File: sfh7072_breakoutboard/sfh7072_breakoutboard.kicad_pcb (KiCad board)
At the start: 2 copper layers, 28 x 23 mm, 10 parts, among them J1 Conn_01x04_Pin, J2 Conn_01x05_Pin

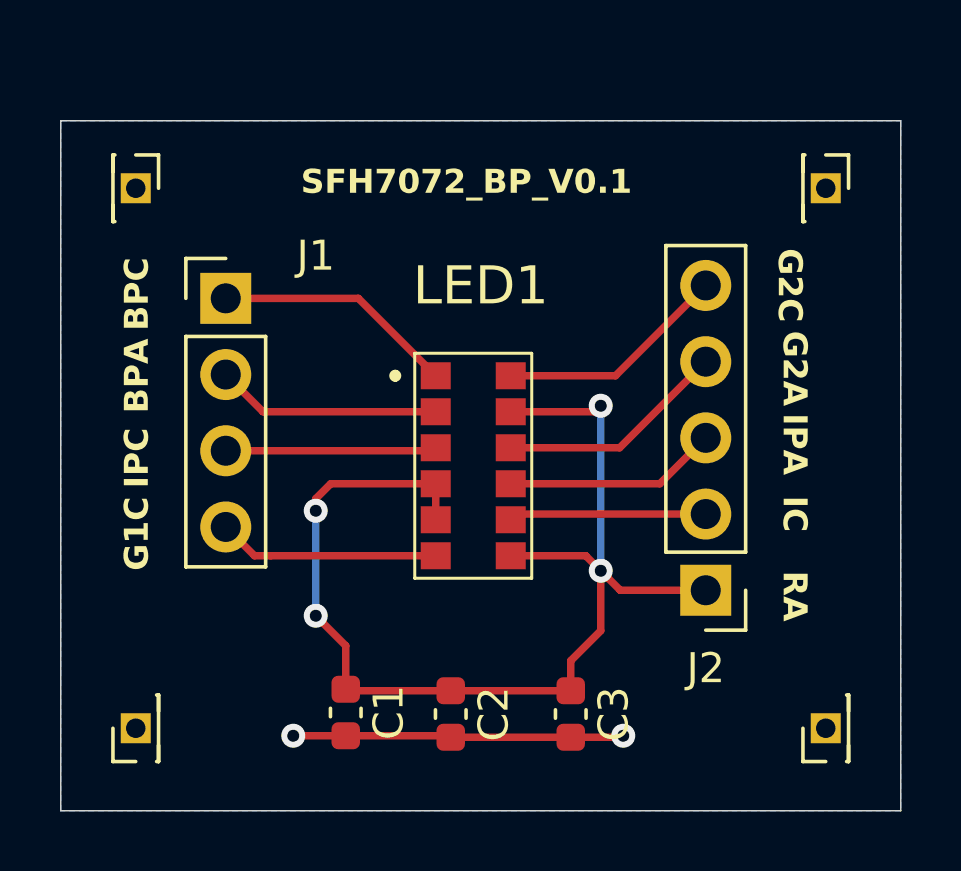
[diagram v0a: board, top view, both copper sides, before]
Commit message: sfh7072 cap location updates
Signed-off-by: Mika Laitio <lamikr@gmail.com>
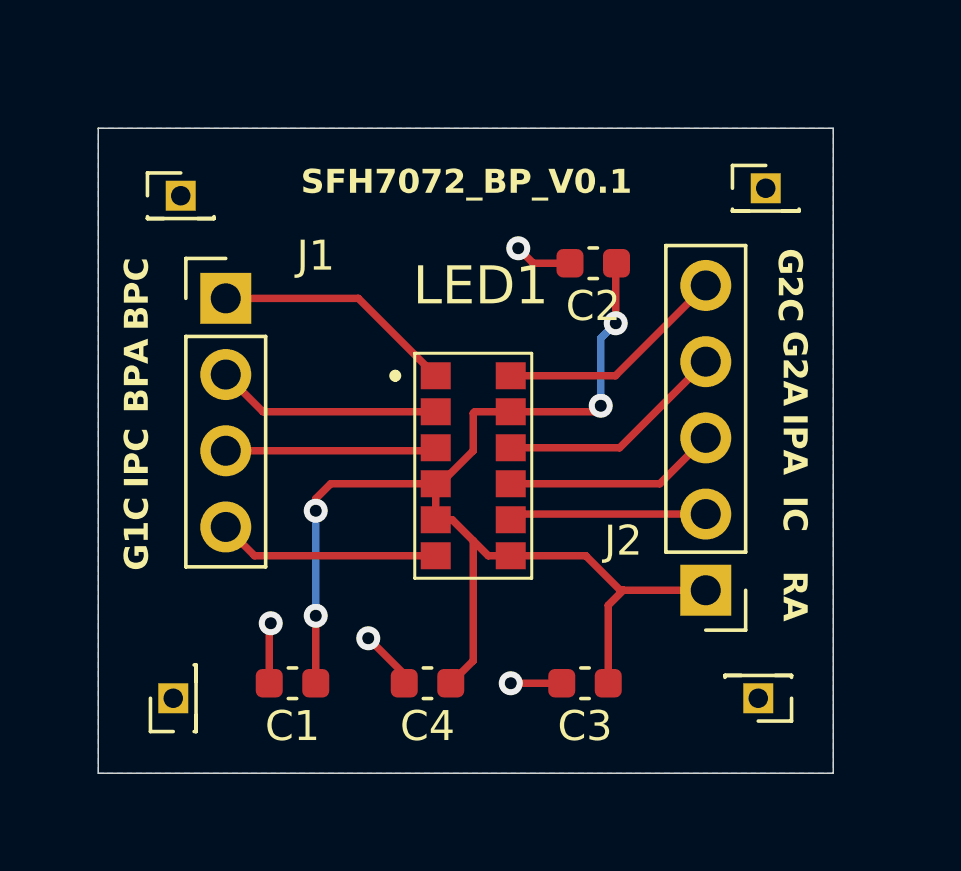
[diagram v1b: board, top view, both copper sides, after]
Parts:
- added C4: 4u7F, Capacitor_SMD:C_0603_1608Metric, F.Cu at (30.7, 35.5)
- moved C2 15.8 mm to (36.2, 21.5), turned to 180 degrees
- moved H3 2.46 mm to (41.8, 36.0), turned to 180 degrees
- moved C1 2.03 mm to (26.2, 35.5), turned to 180 degrees
- moved H2 2.00 mm to (42.0, 19.0), turned to 0 degrees
- moved H4 1.60 mm to (22.2, 36.0)
- moved H1 1.52 mm to (22.5, 19.2), turned to 0 degrees
- moved C3 1.13 mm to (36.0, 35.5), turned to 180 degrees
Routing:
- net GND: track 11.0 -> 7.65 mm, vias 2 -> 4
- net Net-(J2-Pin_1): track 39.7 -> 42.2 mm
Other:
- board size 28 x 23 mm -> 24.5 x 21.5 mm

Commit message: sfh7072 breakoutboard and pcb manufacturing
Signed-off-by: Mika Laitio <lamikr@gmail.com>
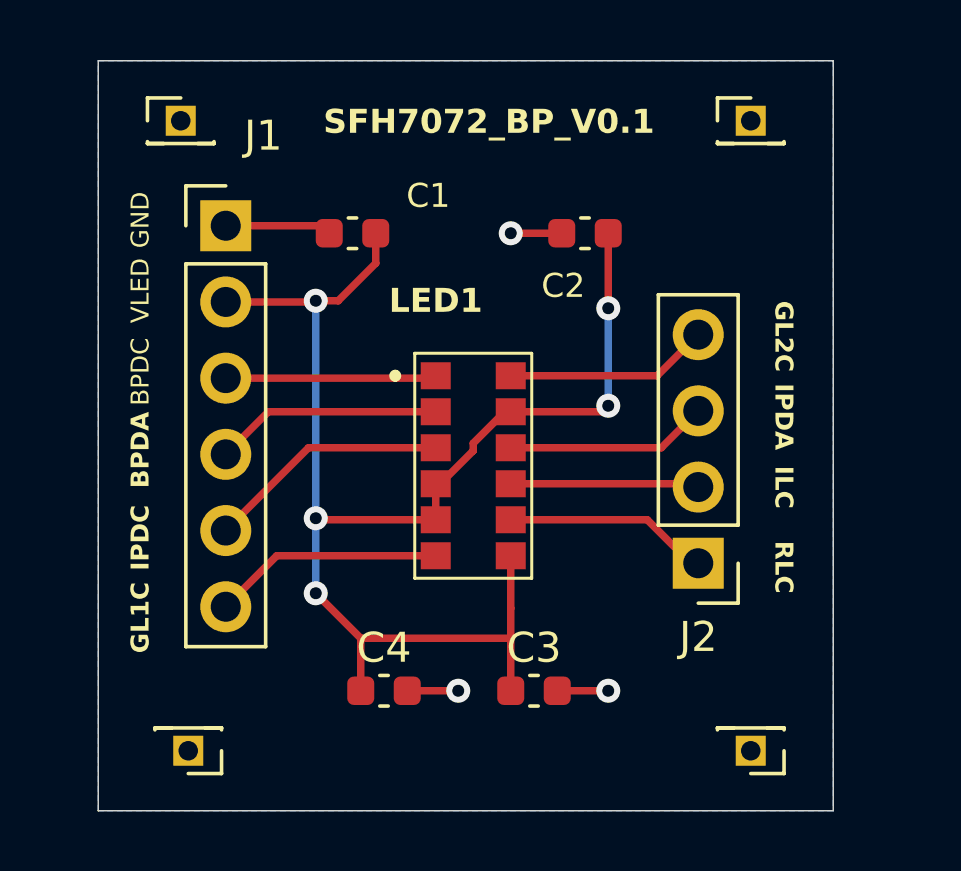
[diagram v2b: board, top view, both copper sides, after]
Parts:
- J1: value Conn_01x04_Pin -> C_01x06; footprint Connector_PinHeader_2.54mm:PinHeader_1x04_P2.54mm_Vertical -> Connector_PinHeader_2.54mm:PinHeader_1x06_P2.54mm_Vertical
- J2: value Conn_01x05_Pin -> C_01x04; footprint Connector_PinHeader_2.54mm:PinHeader_1x05_P2.54mm_Vertical -> Connector_PinHeader_2.54mm:PinHeader_1x04_P2.54mm_Vertical
- moved C1 15.1 mm to (28.2, 20.5)
- moved H1 2.50 mm to (22.5, 16.8)
- moved J1 2.42 mm to (24.0, 20.2)
- moved H2 2.30 mm to (41.5, 16.8)
- moved H4 1.82 mm to (22.8, 37.8), turned to 180 degrees
- moved H3 1.77 mm to (41.5, 37.8)
- moved C3 1.72 mm to (34.3, 35.8), turned to 0 degrees
- moved C4 1.47 mm to (29.3, 35.8), turned to 0 degrees
- moved C2 1.04 mm to (36.0, 20.5)
- moved J2 0.93 mm to (39.8, 31.5)
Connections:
- C1 pad 1: Net-(J2-Pin_1) -> EXT_LED_VSUPPLY
- C2 pad 1: Net-(J2-Pin_1) -> EXT_LED_VSUPPLY
- C3 pad 1: Net-(J2-Pin_1) -> EXT_LED_VSUPPLY
- C4 pad 1: Net-(J2-Pin_1) -> EXT_LED_VSUPPLY
- J1 pad 1: Net-(J1-Pin_1) -> GND
- J1 pad 2: Net-(J1-Pin_2) -> EXT_LED_VSUPPLY
- J1 pad 3: Net-(J1-Pin_3) -> EXT_BROADB_PD_C
- J1 pad 4: Net-(J1-Pin_4) -> EXT_BROADB_PD_A
- J2 pad 1: Net-(J2-Pin_1) -> EXT_RED_LED_C
- J2 pad 2: Net-(J2-Pin_2) -> EXT_IRDA_LED_C
- J2 pad 3: Net-(J2-Pin_3) -> EXT_IRDA_PD_A
- J2 pad 4: Net-(J2-Pin_4) -> EXT_GR_LED2_C
- LED1 pad 1: Net-(J1-Pin_1) -> EXT_BROADB_PD_C
- LED1 pad 10: Net-(J2-Pin_4) -> EXT_IRDA_PD_A
- LED1 pad 11: Net-(J2-Pin_1) -> EXT_LED_VSUPPLY
- LED1 pad 12: Net-(J2-Pin_5) -> EXT_GR_LED2_C
- LED1 pad 2: Net-(J1-Pin_2) -> EXT_BROADB_PD_A
- LED1 pad 3: Net-(J1-Pin_3) -> EXT_IRDA_PD_C
- LED1 pad 4: Net-(J2-Pin_1) -> EXT_LED_VSUPPLY
- LED1 pad 5: Net-(J2-Pin_1) -> EXT_LED_VSUPPLY
- LED1 pad 6: Net-(J1-Pin_4) -> EXT_GR_LED1_C
- LED1 pad 7: Net-(J2-Pin_1) -> EXT_LED_VSUPPLY
- LED1 pad 8: Net-(J2-Pin_2) -> EXT_RED_LED_C
- LED1 pad 9: Net-(J2-Pin_3) -> EXT_IRDA_LED_C
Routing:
- net EXT_LED_VSUPPLY: track 0.00 -> 47.7 mm, vias 0 -> 5
- net Net-(J2-Pin_1): track 42.2 -> 0.00 mm, vias 4 -> 0
- net EXT_IRDA_PD_C: track 0.00 -> 8.28 mm
- net Net-(J1-Pin_1): track 8.07 -> 0.00 mm
- net Net-(J2-Pin_5): track 7.75 -> 0.00 mm
- net EXT_GR_LED1_C: track 0.00 -> 7.70 mm
- net Net-(J2-Pin_4): track 7.69 -> 0.00 mm
- net EXT_BROADB_PD_A: track 0.00 -> 7.59 mm
- net Net-(J1-Pin_2): track 7.51 -> 0.00 mm
- net Net-(J1-Pin_4): track 7.40 -> 0.00 mm
- net Net-(J2-Pin_3): track 7.13 -> 0.00 mm
- net Net-(J1-Pin_3): track 7.04 -> 0.00 mm
- net EXT_BROADB_PD_C: track 0.00 -> 7.03 mm
- net EXT_RED_LED_C: track 0.00 -> 6.85 mm
- net EXT_GR_LED2_C: track 0.00 -> 6.82 mm
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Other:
- board size 24.5 x 21.5 mm -> 24.5 x 25 mm
- board text added: "BPDA"
- board text added: "BPDC"
- board text added: "GL1C"
- board text added: "GL2C"
- board text added: "GND"
- board text added: "ILC"
- board text added: "IPDA"
- board text added: "IPDC"
- board text added: "RLC"
- board text added: "VLED"
- board text removed: "BPA"
- board text removed: "BPC"
- board text removed: "G1C"
- board text removed: "G2A"
- board text removed: "G2C"
- board text removed: "IC"
- board text removed: "IPA"
- board text removed: "IPC"
- board text removed: "RA"
